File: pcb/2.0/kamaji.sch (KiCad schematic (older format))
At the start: 51 parts, among them J1 RJ10, J2 RJ10, J3 RJ10, J4 RJ10, J5 RJ10, J6 RJ10, J7 USB_B, J8 USB_A, Q1 2N3904, Q2 IRL540N, Q3 IRL540N, SW1 SW_Push, SW2 SW_Push, SW3 SW_Push, U1 ATMEGA32U4-AU, Y1 16MHz

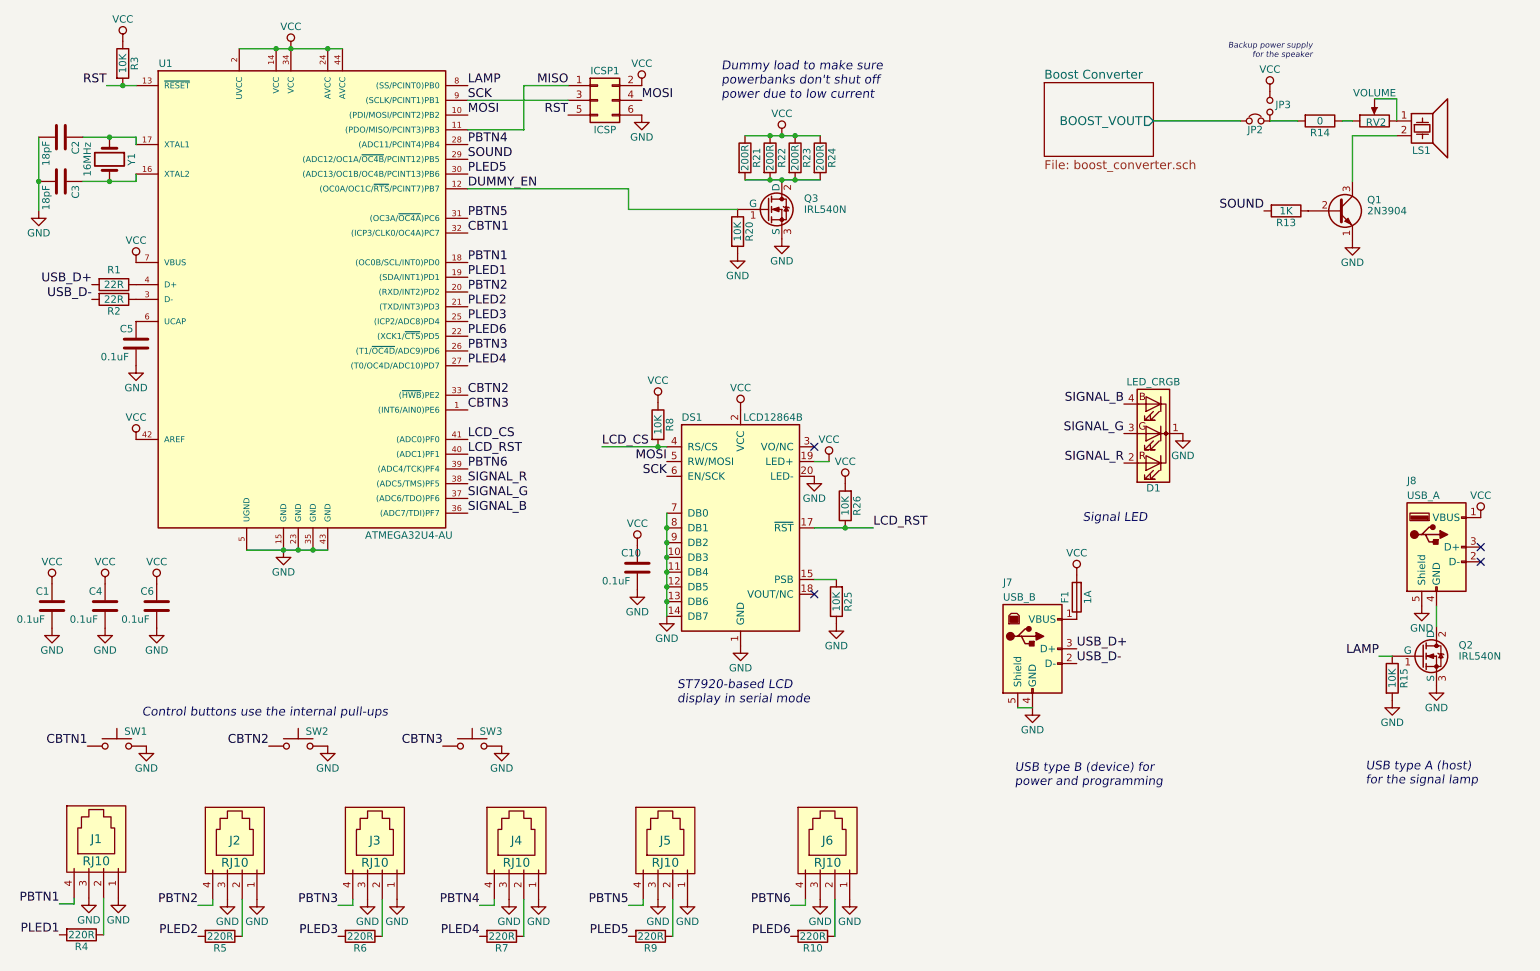
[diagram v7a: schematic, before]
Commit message: first attempt at laying out the 2.0 pcb
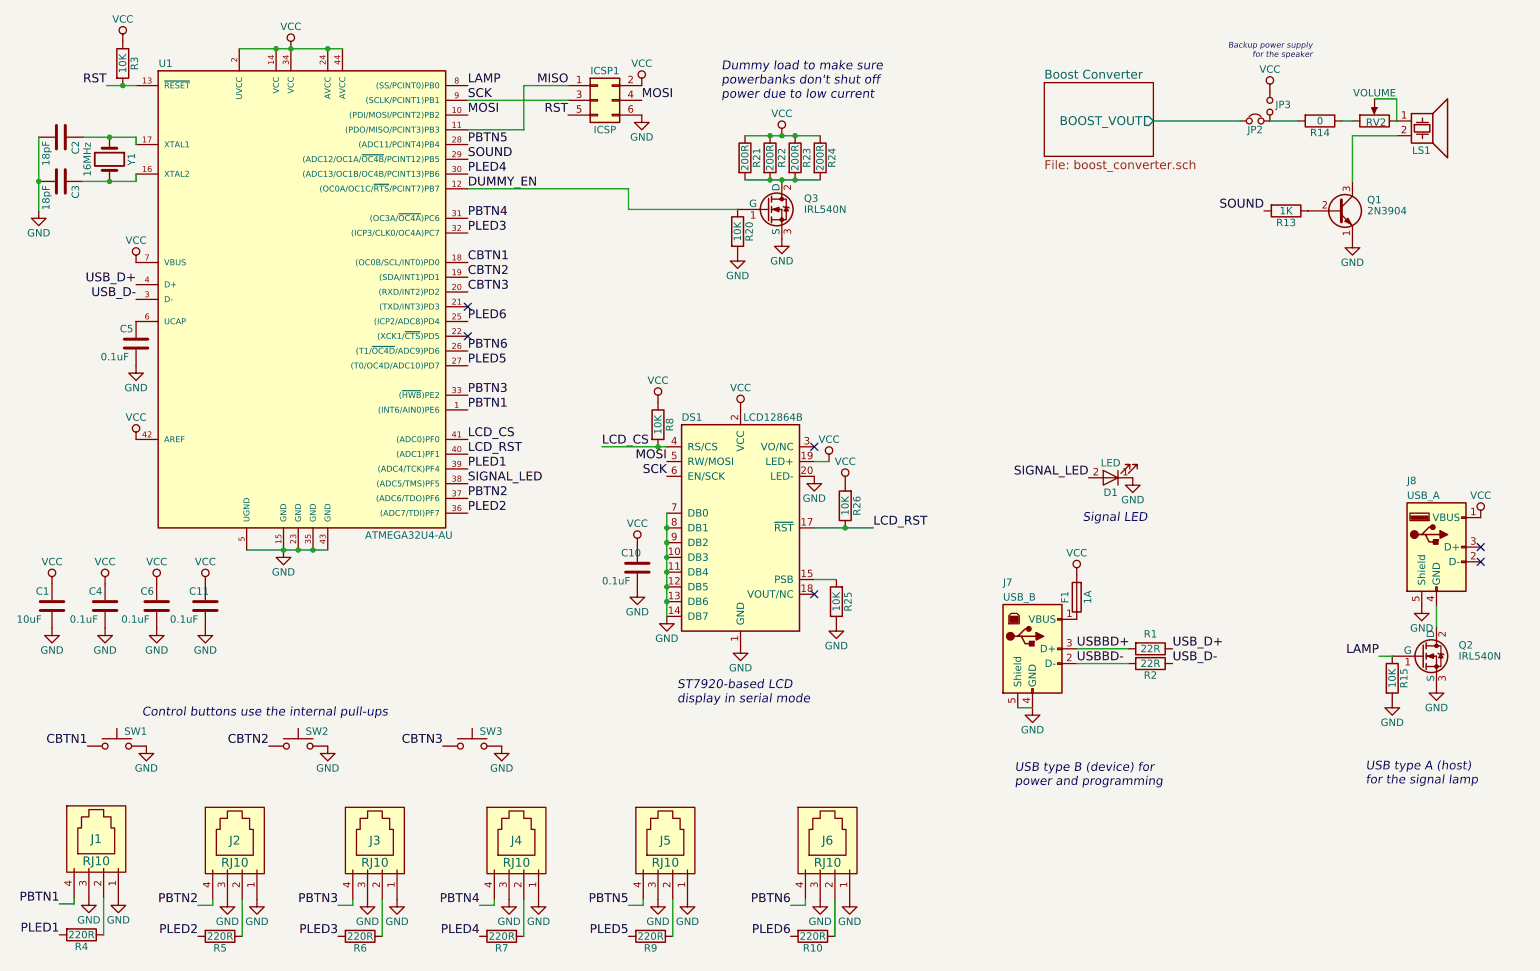
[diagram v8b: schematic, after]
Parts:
- removed D1: LED_CRGB, kamaji:LED_RGB_common_cathode_5mm, symbol LED_CRGB
- added C11: 0.1uF, Capacitors_SMD:C_1206_HandSoldering, symbol C
- added D1: LED, LEDs:LED_D5.0mm, symbol LED
- C1: renamed from C6; value 0.1uF -> 10uF
- renumbered C1 to C6
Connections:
- net SIGNAL_B is gone; now on net PLED2: U1.36 ((ADC7/TDI)PF7)
- net SIGNAL_G is gone; now on net PBTN2: U1.37 ((ADC6/TDO)PF6)
- net CBTN1: now also U1.18 ((OC0B/SCL/INT0)PD0); no longer U1.32 ((ICP3/CLK0/OC4A)PC7)
- net CBTN2: now also U1.19 ((SDA/INT1)PD1); no longer U1.33 ((~HWB~)PE2)
- net CBTN3: now also U1.20 ((RXD/INT2)PD2); no longer U1.1 ((INT6/AIN0)PE6)
- net GND: now also C11.2, D1.1 (K)
- net PBTN1: now also U1.1 ((INT6/AIN0)PE6); no longer U1.18 ((OC0B/SCL/INT0)PD0)
- net PBTN2: no longer U1.20 ((RXD/INT2)PD2)
- net PBTN3: now also U1.33 ((~HWB~)PE2); no longer U1.26 ((T1/~OC4D~/ADC9)PD6)
- net PBTN4: now also U1.31 ((OC3A/~OC4A~)PC6); no longer U1.28 ((ADC11/PCINT4)PB4)
- net PBTN5: now also U1.28 ((ADC11/PCINT4)PB4); no longer U1.31 ((OC3A/~OC4A~)PC6)
- net PBTN6: now also U1.26 ((T1/~OC4D~/ADC9)PD6); no longer U1.39 ((ADC4/TCK)PF4)
- net PLED1: now also U1.39 ((ADC4/TCK)PF4); no longer U1.19 ((SDA/INT1)PD1)
- net PLED2: no longer U1.21 ((TXD/INT3)PD3)
- net PLED3: now also U1.32 ((ICP3/CLK0/OC4A)PC7); no longer U1.25 ((ICP2/ADC8)PD4)
- net PLED4: now also U1.30 ((ADC13/OC1B/OC4B/PCINT13)PB6); no longer U1.27 ((T0/OC4D/ADC10)PD7)
- net PLED5: now also U1.27 ((T0/OC4D/ADC10)PD7); no longer U1.30 ((ADC13/OC1B/OC4B/PCINT13)PB6)
- net PLED6: now also U1.25 ((ICP2/ADC8)PD4); no longer U1.22 ((XCK1/~CTS~)PD5)
- net USB_D+: now also R1.1, U1.4 (D+); no longer J7.3 (D+), R1.2
- net USB_D-: now also R2.1, U1.3 (D-); no longer J7.2 (D-), R2.2
- net VCC: now also C11.1
- net SIGNAL_R renamed SIGNAL_LED
- net SIGNAL_LED: now also D1.2 (A)
- new net USBBD+: J7.3 (D+), R1.2
- new net USBBD-: J7.2 (D-), R2.2
- no-connect marks 4 -> 6
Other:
- moved on the sheet: C1, C6, R1, R2
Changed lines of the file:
@@
 L R R1
 U 1 1 59E8EF8C
-P 1330 2830
-F 0 "R1" V 1230 2830 50  0000 C CNN
-F 1 "22R" V 1330 2830 50  0000 C CNN
-F 2 "Resistors_SMD:R_1206_HandSoldering" V 1260 2830 50  0001 C CNN
-F 3 "" H 1330 2830 50  0001 C CNN
-	1    1330 2830
+P 8360 5300
+F 0 "R1" V 8260 5300 50  0000 C CNN
+F 1 "22R" V 8360 5300 50  0000 C CNN
+F 2 "Resistors_SMD:R_1206_HandSoldering" V 8290 5300 50  0001 C CNN
+F 3 "" H 8360 5300 50  0001 C CNN
+	1    8360 5300
 	0    1    1    0
 $EndComp
@@
 L R R2
 U 1 1 59E8F0DD
-P 1330 2930
-F 0 "R2" V 1410 2930 50  0000 C CNN
-F 1 "22R" V 1330 2930 50  0000 C CNN
-F 2 "Resistors_SMD:R_1206_HandSoldering" V 1260 2930 50  0001 C CNN
-F 3 "" H 1330 2930 50  0001 C CNN
-	1    1330 2930
+P 8360 5400
+F 0 "R2" V 8440 5400 50  0000 C CNN
+F 1 "22R" V 8360 5400 50  0000 C CNN
+F 2 "Resistors_SMD:R_1206_HandSoldering" V 8290 5400 50  0001 C CNN
+F 3 "" H 8360 5400 50  0001 C CNN
+	1    8360 5400
 	0    1    1    0
 $EndComp
@@
 USB type A (host)\nfor the signal lamp
 $Comp
-L C C1
+L C C6
 U 1 1 59EB7B64
-P 910 5010
-F 0 "C1" H 800 5110 50  0000 L CNN
-F 1 "0.1uF" H 670 4920 50  0000 L CNN
-F 2 "Capacitors_SMD:C_1206_HandSoldering" H 948 4860 50  0001 C CNN
-F 3 "" H 910 5010 50  0001 C CNN
-	1    910  5010
+P 1620 5010
+F 0 "C6" H 1510 5110 50  0000 L CNN
+F 1 "0.1uF" H 1380 4920 50  0000 L CNN
+F 2 "Capacitors_SMD:C_1206_HandSoldering" H 1658 4860 50  0001 C CNN
+F 3 "" H 1620 5010 50  0001 C CNN
+	1    1620 5010
 	1    0    0    -1
 $EndComp
@@
 $EndComp
 $Comp
-L C C6
+L C C1
 U 1 1 5A15E885
-P 1620 5010
-F 0 "C6" H 1510 5110 50  0000 L CNN
-F 1 "0.1uF" H 1380 4920 50  0000 L CNN
-F 2 "Capacitors_SMD:C_1206_HandSoldering" H 1658 4860 50  0001 C CNN
-F 3 "" H 1620 5010 50  0001 C CNN
-	1    1620 5010
+P 910 5010
+F 0 "C1" H 800 5110 50  0000 L CNN
+F 1 "10uF" H 670 4920 50  0000 L CNN
+F 2 "Capacitors_SMD:C_1206_HandSoldering" H 948 4860 50  0001 C CNN
+F 3 "" H 910 5010 50  0001 C CNN
+	1    910  5010
 	1    0    0    -1
 $EndComp
@@
 Text Label 3730 1680 0    60   ~ 0
 MOSI
-Text Label 3730 3080 0    60   ~ 0
+Text Label 3730 2480 0    60   ~ 0
 PLED3
+Text Label 3730 2380 0    60   ~ 0
+PBTN4
+Text Label 3730 2080 0    60   ~ 0
+PLED4
 Text Label 3730 1880 0    60   ~ 0
-PBTN4
+PBTN5
 Text Label 3730 3380 0    60   ~ 0
-PLED4
-Text Label 3730 2380 0    60   ~ 0
-PBTN5
-Text Label 3730 2080 0    60   ~ 0
 PLED5
 Text Label 4410 1680 2    60   ~ 0
 RST
+Text Label 3730 3680 0    60   ~ 0
+PBTN1
+Text Label 3730 4080 0    60   ~ 0
+PLED1
+Text Label 3730 4280 0    60   ~ 0
+PBTN2
 Text Label 3730 2680 0    60   ~ 0
-PBTN1
+CBTN1
+Text Label 3730 4380 0    60   ~ 0
+PLED2
+Text Label 3730 3580 0    60   ~ 0
+PBTN3
 Text Label 3730 2780 0    60   ~ 0
-PLED1
+CBTN2
 Text Label 3730 2880 0    60   ~ 0
-PBTN2
-Text Label 3730 2480 0    60   ~ 0
-CBTN1
-Text Label 3730 2980 0    60   ~ 0
-PLED2
-Text Label 3730 3280 0    60   ~ 0
-PBTN3
-Text Label 3730 3580 0    60   ~ 0
-CBTN2
-Text Label 3730 3680 0    60   ~ 0
 CBTN3
 Text Label 5080 4130 2    60   ~ 0
@@
 Text Label 1280 1480 2    60   ~ 0
 RST
-Text Label 1180 2830 2    60   ~ 0
+Text Label 1480 2830 2    60   ~ 0
 USB_D+
-Text Label 1180 2930 2    60   ~ 0
+Text Label 1480 2930 2    60   ~ 0
 USB_D-
 Text Label 1150 5960 2    60   ~ 0
@@
 Text Label 3560 5960 2    60   ~ 0
 CBTN3
-Text Label 7860 5300 0    60   ~ 0
+Text Label 8510 5300 0    60   ~ 0
 USB_D+
-Text Label 7860 5400 0    60   ~ 0
+Text Label 8510 5400 0    60   ~ 0
 USB_D-
 Text Label 9910 5350 2    60   ~ 0
@@
 	1    0    0    -1
 $EndComp
-Text Label 3730 4180 0    60   ~ 0
-SIGNAL_R
-Text Label 3730 4280 0    60   ~ 0
-SIGNAL_G
-Text Label 3730 4380 0    60   ~ 0
-SIGNAL_B
 $Comp
 L GND #PWR050
@@
 Text Label 5920 7250 2    60   ~ 0
 PLED6
-Text Label 3730 4080 0    60   ~ 0
+Text Label 3730 3280 0    60   ~ 0
 PBTN6
-Text Label 3730 3180 0    60   ~ 0
+Text Label 3730 3080 0    60   ~ 0
 PLED6
+Text Notes 7900 4450 0    60   Italic 0
+Signal LED
+$Sheet
+S 7640 1460 740  500
+U 5A30C66D
+F0 "Boost Converter" 60
+F1 "boost_converter.sch" 60
+F2 "BOOST_VOUT" O R 8380 1720 60
+$EndSheet
+$Comp
+L C C11
+U 1 1 5A3B9847
+P 1950 5010
+F 0 "C11" H 1840 5110 50  0000 L CNN
+F 1 "0.1uF" H 1710 4920 50  0000 L CNN
+F 2 "Capacitors_SMD:C_1206_HandSoldering" H 1988 4860 50  0001 C CNN
+F 3 "" H 1950 5010 50  0001 C CNN
+	1    1950 5010
+	1    0    0    -1
+$EndComp
+$Comp
+L GND #PWR052
+U 1 1 5A3B984D
+P 1950 5160
+F 0 "#PWR052" H 1950 4910 50  0001 C CNN
+F 1 "GND" H 1950 5010 50  0000 C CNN
+F 2 "" H 1950 5160 50  0001 C CNN
+F 3 "" H 1950 5160 50  0001 C CNN
+	1    1950 5160
+	1    0    0    -1
+$EndComp
+$Comp
+L VCC #PWR053
+U 1 1 5A3B9853
+P 1950 4860
+F 0 "#PWR053" H 1950 4710 50  0001 C CNN
+F 1 "VCC" H 1950 5010 50  0000 C CNN
+F 2 "" H 1950 4860 50  0001 C CNN
+F 3 "" H 1950 4860 50  0001 C CNN
+	1    1950 4860
+	1    0    0    -1
+$EndComp
 Wire Wire Line
 	2180 1230 2880 1230
@@
 Wire Wire Line
 	5920 7040 6020 7040
-$Comp
-L LED_CRGB D1
-U 1 1 5A3AC970
-P 8380 3840
-F 0 "D1" H 8380 4210 50  0000 C CNN
-F 1 "LED_CRGB" H 8380 3490 50  0000 C CNN
-F 2 "kamaji:LED_RGB_common_cathode_5mm" H 8380 3790 50  0001 C CNN
-F 3 "" H 8380 3790 50  0001 C CNN
-	1    8380 3840
+Wire Wire Line
+	8380 1720 8970 1720
+Text Label 7860 5300 0    60   ~ 0
+USBBD+
+Text Label 7860 5400 0    60   ~ 0
+USBBD-
+Wire Wire Line
+	7860 5300 8210 5300
+Wire Wire Line
+	7860 5400 8210 5400
+$Comp
+L LED D1
+U 1 1 5A3C1B55
+P 8090 4140
+F 0 "D1" H 8090 4240 50  0000 C CNN
+F 1 "LED" H 8090 4040 50  0000 C CNN
+F 2 "LEDs:LED_D5.0mm" H 8090 4140 50  0001 C CNN
+F 3 "" H 8090 4140 50  0001 C CNN
+	1    8090 4140
 	-1   0    0    1
 $EndComp
-Text Notes 7900 4450 0    60   Italic 0
-Signal LED
-$Comp
-L GND #PWR052
-U 1 1 5A3ACD5F
-P 8580 3840
-F 0 "#PWR052" H 8580 3590 50  0001 C CNN
-F 1 "GND" H 8580 3690 50  0000 C CNN
-F 2 "" H 8580 3840 50  0001 C CNN
-F 3 "" H 8580 3840 50  0001 C CNN
-	1    8580 3840
-	1    0    0    -1
-$EndComp
-Text Label 8180 4040 2    60   ~ 0
-SIGNAL_R
-Text Label 8180 3840 2    60   ~ 0
-SIGNAL_G
-Text Label 8180 3640 2    60   ~ 0
-SIGNAL_B
-$Sheet
-S 7640 1460 740  500
-U 5A30C66D
-F0 "Boost Converter" 60
-F1 "boost_converter.sch" 60
-F2 "BOOST_VOUT" O R 8380 1720 60
-$EndSheet
-Wire Wire Line
-	8380 1720 8970 1720
+$Comp
+L GND #PWR054
+U 1 1 5A3C2004
+P 8240 4140
+F 0 "#PWR054" H 8240 3890 50  0001 C CNN
+F 1 "GND" H 8240 3990 50  0000 C CNN
+F 2 "" H 8240 4140 50  0001 C CNN
+F 3 "" H 8240 4140 50  0001 C CNN
+	1    8240 4140
+	1    0    0    -1
+$EndComp
+Text Label 7940 4140 2    60   ~ 0
+SIGNAL_LED
+Text Label 3730 4180 0    60   ~ 0
+SIGNAL_LED
+NoConn ~ 3730 2980
+NoConn ~ 3730 3180
 $EndSCHEMATC
